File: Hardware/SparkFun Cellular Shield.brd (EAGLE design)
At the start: 53.3 x 73.7 mm, 29 parts, among them U1 ARDUINO_R3_SHIELD, U2 SPX29302, U3 SM5100B, U4 SIMHOLDER3

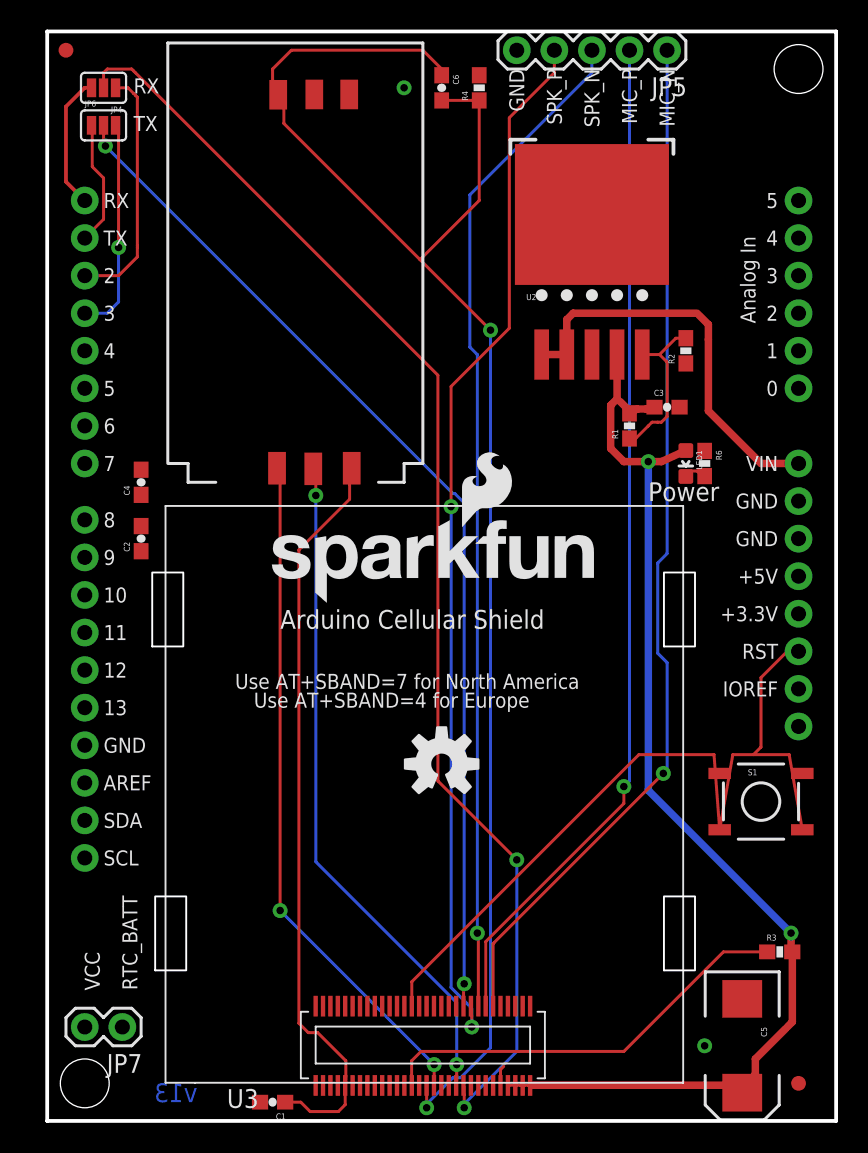
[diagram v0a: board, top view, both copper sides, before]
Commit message: Board layout cleanup
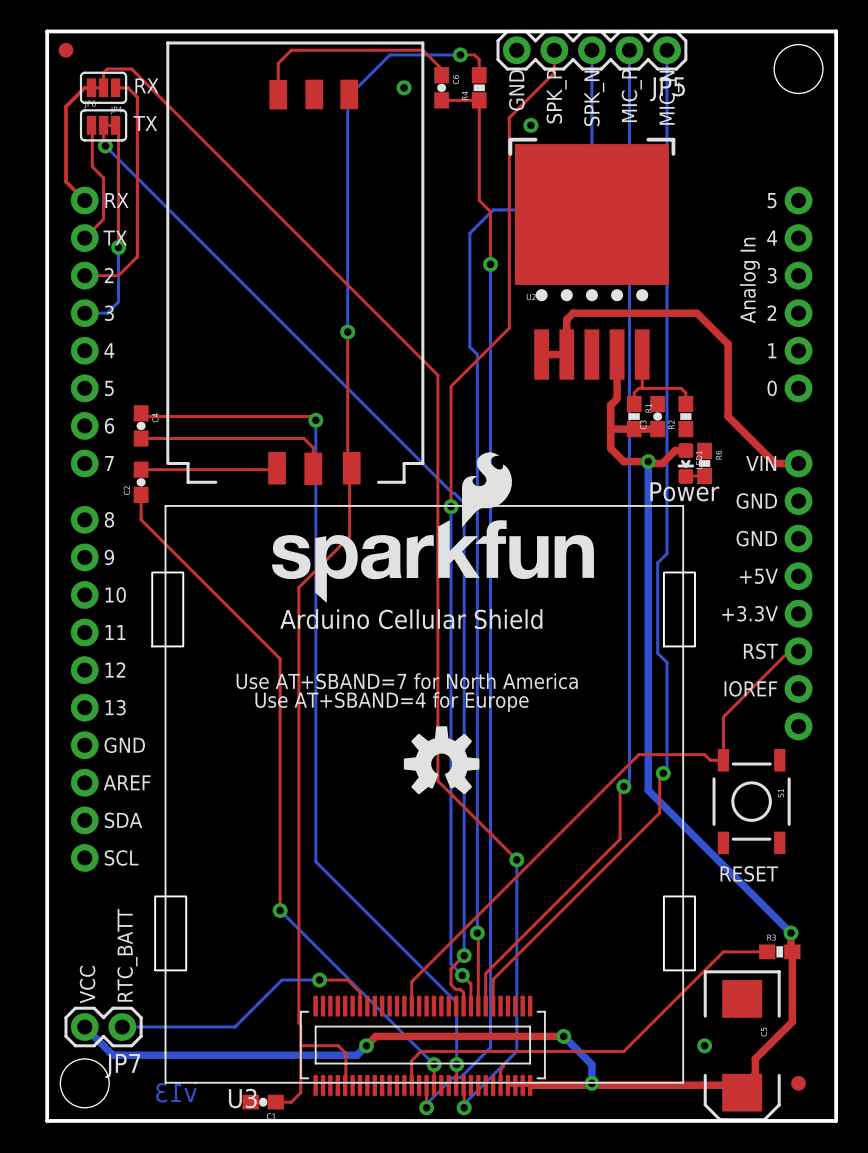
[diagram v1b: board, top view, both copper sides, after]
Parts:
- JP4, JP6: value JUMPER-PAD-3-2OF3_NC_BY_PASTE -> JUMPER-PAD-3-2OF3_NC_BY_TRACE_SMALL; device SparkFun-Passives:PAD-JUMPER-3-2OF3_NC_BY_PASTE_YES_SILK_FULL_BOX -> SparkFun-Passives:PAD-JUMPER-3-2OF3_NC_BY_TRACE_YES_SILK_FULL_BOX
- moved R2 4.45 mm to (43.2, 47.6)
- moved C2 3.81 mm to (6.35, 43.2)
- moved C4 3.81 mm to (6.35, 47.0), turned to 270 degrees
- moved C3 0.90 mm to (41.3, 47.6), turned to 90 degrees
- moved R1 0.71 mm to (39.7, 47.6), turned to 270 degrees
- moved C1 0.63 mm to (14.6, 1.27)
- moved S1 0.63 mm to (47.6, 21.6), turned to 270 degrees
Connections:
- net GND: no longer S1.2
- net RESET: no longer S1.4
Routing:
- net VCC: track 79.2 -> 117.4 mm, vias 2 -> 5
- net SIM_VCC: track 50.7 -> 87.5 mm, vias 0 -> 2
- net RTC_BATT: track 0.00 -> 18.7 mm, vias 0 -> 1
- net SIM_IO: track 91.9 -> 74.6 mm
- net RESET: track 56.4 -> 39.1 mm
- net SIM_RST: track 44.6 -> 60.9 mm
- net N$2: track 0.00 -> 13.3 mm
- net N$3: track 0.00 -> 9.23 mm
- net ADJUST: track 11.0 -> 7.55 mm
- net SPK_N: track 68.3 -> 71.6 mm
- net SIM_CLK: track 45.0 -> 48.1 mm
- net SPK_P: track 70.9 -> 68.1 mm
- net RXD0: track 69.7 -> 70.6 mm
- net VRAW: track 27.5 -> 27.0 mm
- net GND: vias 2 -> 3
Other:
- board text added: "RESET"

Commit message: Additional part updates, adding dimensions
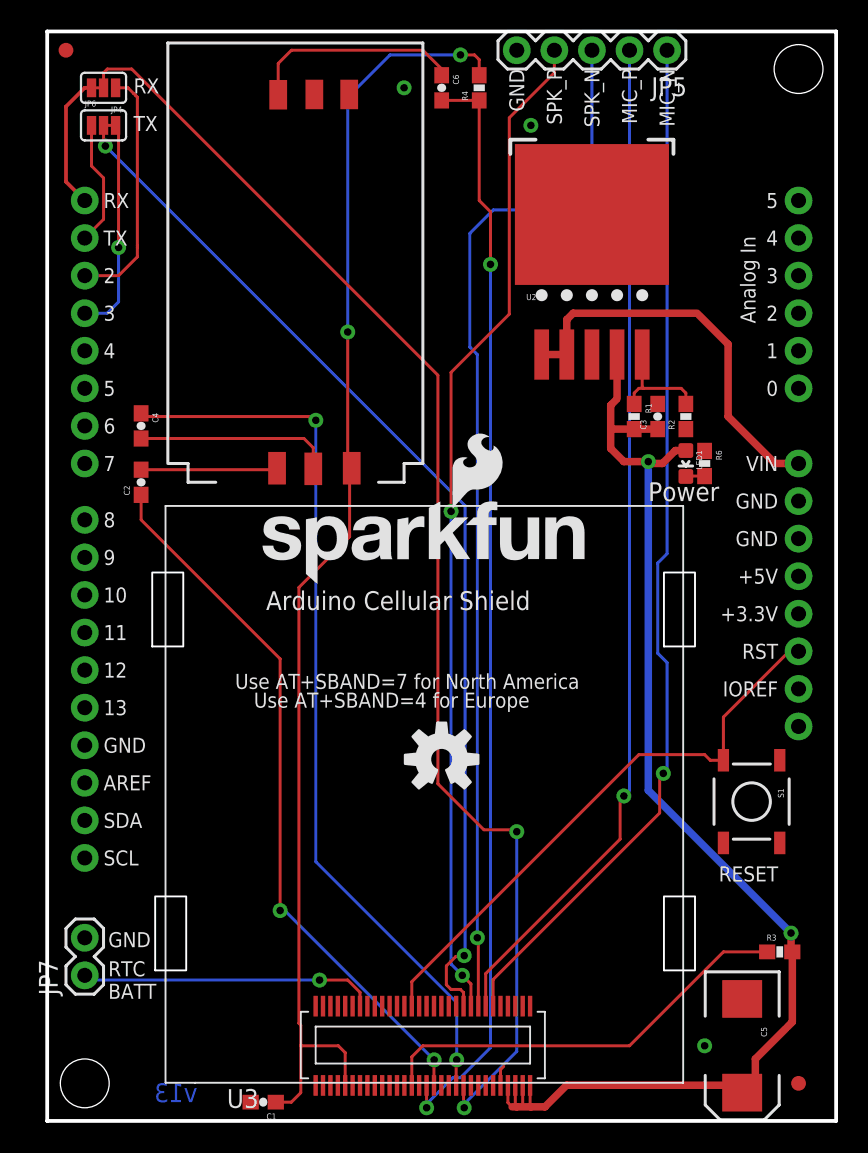
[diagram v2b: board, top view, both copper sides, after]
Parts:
- moved JP7 4.32 mm to (2.54, 9.84), turned to 90 degrees
- moved JP1 1.42 mm to (13.8, 36.2)
- moved LOGO1 0.32 mm to (26.7, 24.4)
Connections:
- net GND: now also JP7.2
- net VCC: no longer JP7.2
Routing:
- net VCC: track 117.4 -> 86.7 mm, vias 5 -> 2
- net RTC_BATT: track 18.7 -> 20.0 mm
- net TXD0: track 87.0 -> 88.3 mm
- net RXD0: track 70.6 -> 71.4 mm
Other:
- board text added: "RTC BATT"
- board text added: "Ryan Owens"
- board text removed: "Nathan Seidle"
- board text removed: "RTC_BATT"
- board text removed: "VCC"

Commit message: Updating parts with PROD IDs, fixing DRC errors w/ tKeepout on
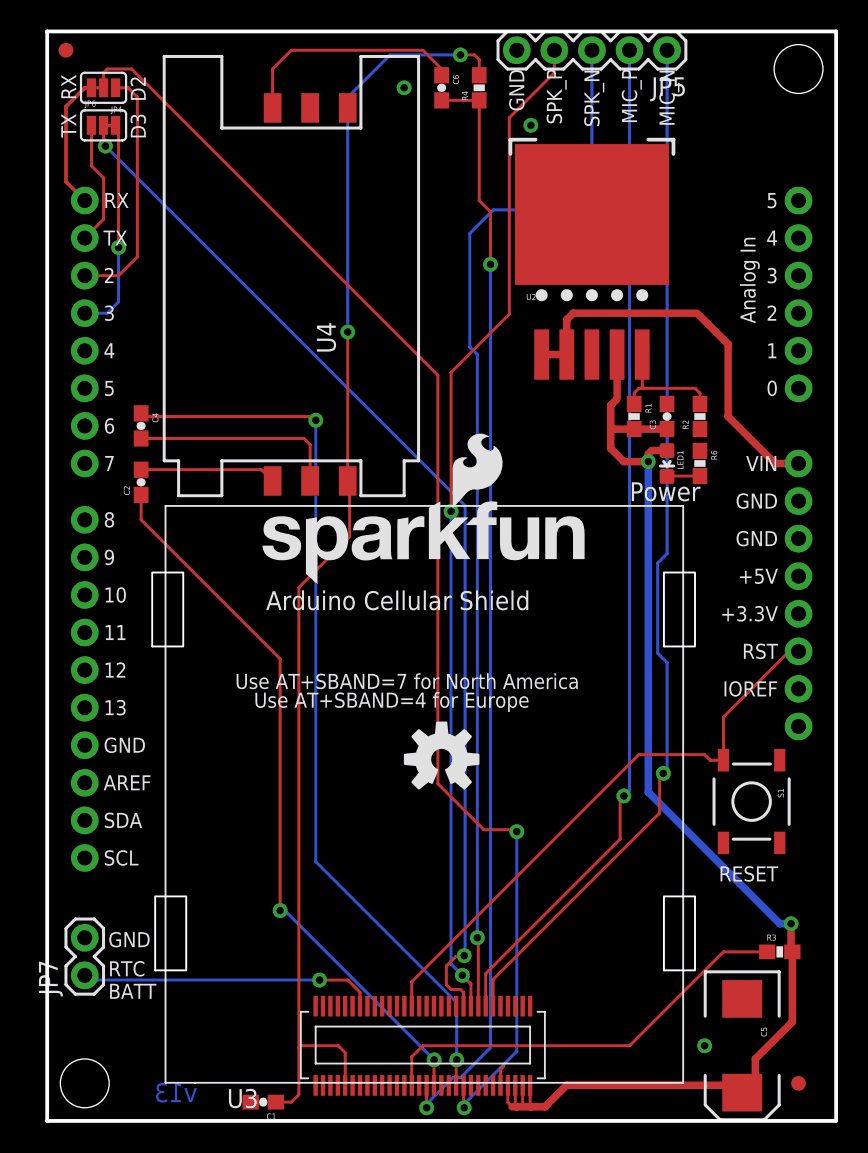
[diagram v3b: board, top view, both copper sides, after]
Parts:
- JP2, JP3: device SparkFun:FIDUCIAL-1X2 -> SparkFun-Aesthetics:FIDUCIAL-1X2
- U3: device SparkFun:SM5100B -> SparkFun-RF:SM5100B
- U4: value SIMHOLDER3 -> (none); device SparkFun:SIMHOLDER3 -> SparkFun-Connectors:SIMHOLDER
- moved U4 15.5 mm to (16.5, 55.9)
- moved LED1 1.27 mm to (41.9, 44.5)
- moved R2 0.95 mm to (44.1, 47.6)
- moved C3 0.63 mm to (41.9, 47.6)
- moved R6 0.32 mm to (44.1, 44.5)
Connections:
- net GND: now also U4.C5; no longer U4.6
- net N$1: now also U4.C7; no longer U4.4
- net N$2: now also U4.C2; no longer U4.2
- net N$3: now also U4.C3; no longer U4.3
- net SIM_VCC: now also U4.C1; no longer U4.1
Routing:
- net N$1: track 14.5 -> 15.5 mm
- net N$17: track 1.28 -> 2.23 mm
- net ADJUST: track 7.55 -> 8.51 mm
- net N$2: track 13.3 -> 14.1 mm
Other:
- board text added: "D2"
- board text added: "D3"

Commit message: Adding in 20mm battery fp for RTC
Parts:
- added BAT1: (no value), SparkFun-Electromechanical:BATTCOM_20MM_PTH
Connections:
- net GND: now also BAT1.2
- net RTC_BATT: now also BAT1.1
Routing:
- net RTC_BATT: track 20.0 -> 40.5 mm
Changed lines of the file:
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@@
 <setting verticaltext="up"/>
 </settings>
-<grid distance="0.0125" unitdist="inch" unit="inch" style="lines" multiple="1" display="yes" altdistance="0.005" altunitdist="inch" altunit="inch"/>
+<grid distance="0.05" unitdist="inch" unit="inch" style="lines" multiple="1" display="yes" altdistance="0.005" altunitdist="inch" altunit="inch"/>
 <layers>
 <layer number="1" name="Top" color="4" fill="1" visible="yes" active="yes"/>
@@
 <layer number="37" name="tTest" color="7" fill="1" visible="no" active="yes"/>
 <layer number="38" name="bTest" color="7" fill="1" visible="no" active="yes"/>
-<layer number="39" name="tKeepout" color="4" fill="11" visible="yes" active="yes"/>
-<layer number="40" name="bKeepout" color="1" fill="11" visible="yes" active="yes"/>
+<layer number="39" name="tKeepout" color="4" fill="11" visible="no" active="yes"/>
+<layer number="40" name="bKeepout" color="1" fill="11" visible="no" active="yes"/>
 <layer number="41" name="tRestrict" color="4" fill="10" visible="no" active="yes"/>
 <layer number="42" name="bRestrict" color="1" fill="10" visible="no" active="yes"/>
@@
 <layer number="47" name="Measures" color="7" fill="1" visible="no" active="yes"/>
 <layer number="48" name="Document" color="7" fill="1" visible="no" active="yes"/>
-<layer number="49" name="Reference" color="7" fill="1" visible="no" active="yes"/>
+<layer number="49" name="Reference" color="7" fill="1" visible="yes" active="yes"/>
 <layer number="50" name="dxf" color="7" fill="1" visible="no" active="yes"/>
 <layer number="51" name="tDocu" color="6" fill="1" visible="yes" active="yes"/>
@@
 <element name="STANDOFF1" library="SparkFun-Electromechanical" package="STAND-OFF" value="STAND-OFF" x="2.54" y="2.54"/>
 <element name="STANDOFF2" library="SparkFun-Electromechanical" package="STAND-OFF" value="STAND-OFF" x="50.8" y="71.12"/>
+<element name="BAT1" library="SparkFun-Electromechanical" package="BATTCOM_20MM_PTH" value="" x="24.13" y="22.86" rot="MR0"/>
 </elements>
 <signals>
@@
 <via x="32.7025" y="67.31" extent="1-16" drill="0.508"/>
 <contactref element="JP7" pad="2"/>
+<contactref element="BAT1" pad="2"/>
 </signal>
 <signal name="VCC">
@@
 <contactref element="U3" pad="5"/>
 <contactref element="R3" pad="2"/>
-<contactref element="C5" pad="A"/>
-<contactref element="U2" pad="4"/>
-<contactref element="R1" pad="2"/>
-<contactref element="C3" pad="1"/>
-<contactref element="LED1" pad="A"/>
 <wire x1="47.879" y1="4.191" x2="49.911" y2="6.223" width="0.508" layer="1"/>
 <wire x1="40.64" y1="22.225" x2="40.64" y2="44.577" width="0.508" layer="16"/>
 <wire x1="50.292" y1="11.938" x2="50.292" y2="13.335" width="0.508" layer="1"/>
-<wire x1="38.53" y1="48.846" x2="38.53" y2="51.815" width="0.508" layer="1"/>
 <wire x1="40.64" y1="44.577" x2="38.989" y2="44.577" width="0.508" layer="1"/>
 <wire x1="38.989" y1="44.577" x2="38.1" y2="45.466" width="0.508" layer="1"/>
@@
 <via x="40.64" y="44.577" extent="1-16" drill="0.508"/>
 <via x="50.292" y="13.335" extent="1-16" drill="0.508"/>
-<wire x1="39.6875" y1="46.775" x2="41.91" y2="46.775" width="0.508" layer="1"/>
-<wire x1="39.6875" y1="46.775" x2="38.2025" y2="46.775" width="0.508" layer="1"/>
 <wire x1="38.2025" y1="46.775" x2="38.1" y2="46.6725" width="0.508" layer="1"/>
 <wire x1="40.767" y1="44.45" x2="40.64" y2="44.577" width="0.508" layer="1"/>
@@
 <wire x1="31.75" y1="0.9525" x2="32.0675" y2="0.9525" width="0.2032" layer="1"/>
 <wire x1="32.0675" y1="0.9525" x2="32.15" y2="1.035" width="0.2032" layer="1"/>
-<wire x1="46.487" y1="2.413" x2="46.99" y2="1.91" width="0.508" layer="1"/>
 <wire x1="47.879" y1="4.191" x2="47.879" y2="2.799" width="0.508" layer="1"/>
-<wire x1="47.879" y1="2.799" x2="46.99" y2="1.91" width="0.508" layer="1"/>
 <wire x1="50.292" y1="11.938" x2="50.292" y2="11.518" width="0.2032" layer="1"/>
 <wire x1="50.292" y1="11.518" x2="50.38" y2="11.43" width="0.2032" layer="1"/>
-<wire x1="35.1155" y1="2.413" x2="46.487" y2="2.413" width="0.508" layer="1"/>
+<wire x1="35.1155" y1="2.413" x2="47.493" y2="2.413" width="0.508" layer="1"/>
 <wire x1="40.64" y1="22.225" x2="49.53" y2="13.335" width="0.508" layer="16"/>
 <wire x1="49.53" y1="13.335" x2="50.292" y2="13.335" width="0.508" layer="16"/>
-<wire x1="41.91" y1="45.327" x2="40.882" y2="45.327" width="0.508" layer="1"/>
 <wire x1="40.882" y1="45.327" x2="40.64" y2="45.085" width="0.508" layer="1"/>
 <wire x1="40.64" y1="45.085" x2="40.64" y2="44.577" width="0.508" layer="1"/>
+<contactref element="C3" pad="1"/>
+<contactref element="LED1" pad="A"/>
+<contactref element="U2" pad="4"/>
+<contactref element="R1" pad="2"/>
+<contactref element="C5" pad="A"/>
+<wire x1="38.53" y1="48.846" x2="38.53" y2="51.815" width="0.508" layer="1"/>
+<wire x1="38.2025" y1="46.775" x2="39.6875" y2="46.775" width="0.508" layer="1"/>
+<wire x1="40.882" y1="45.327" x2="41.91" y2="45.327" width="0.508" layer="1"/>
+<wire x1="41.91" y1="45.327" x2="41.91" y2="46.775" width="0.508" layer="1"/>
+<wire x1="47.493" y1="2.413" x2="47.879" y2="2.799" width="0.508" layer="1"/>
+<wire x1="46.99" y1="1.91" x2="47.493" y2="2.413" width="0.508" layer="1"/>
 </signal>
 <signal name="BOOT">
@@
 <wire x1="18.415" y1="9.525" x2="2.8575" y2="9.525" width="0.2032" layer="16"/>
 <wire x1="2.8575" y1="9.525" x2="2.54" y2="9.8425" width="0.2032" layer="16"/>
+<contactref element="BAT1" pad="1"/>
+<wire x1="12.28" y1="22.86" x2="12.28" y2="14.185" width="0.508" layer="1"/>
+<wire x1="12.28" y1="14.185" x2="7.62" y2="9.525" width="0.508" layer="1"/>
+<wire x1="7.62" y1="9.525" x2="2.8575" y2="9.525" width="0.508" layer="1"/>
+<wire x1="2.8575" y1="9.525" x2="2.54" y2="9.8425" width="0.508" layer="1"/>
 </signal>
 <signal name="N$1">

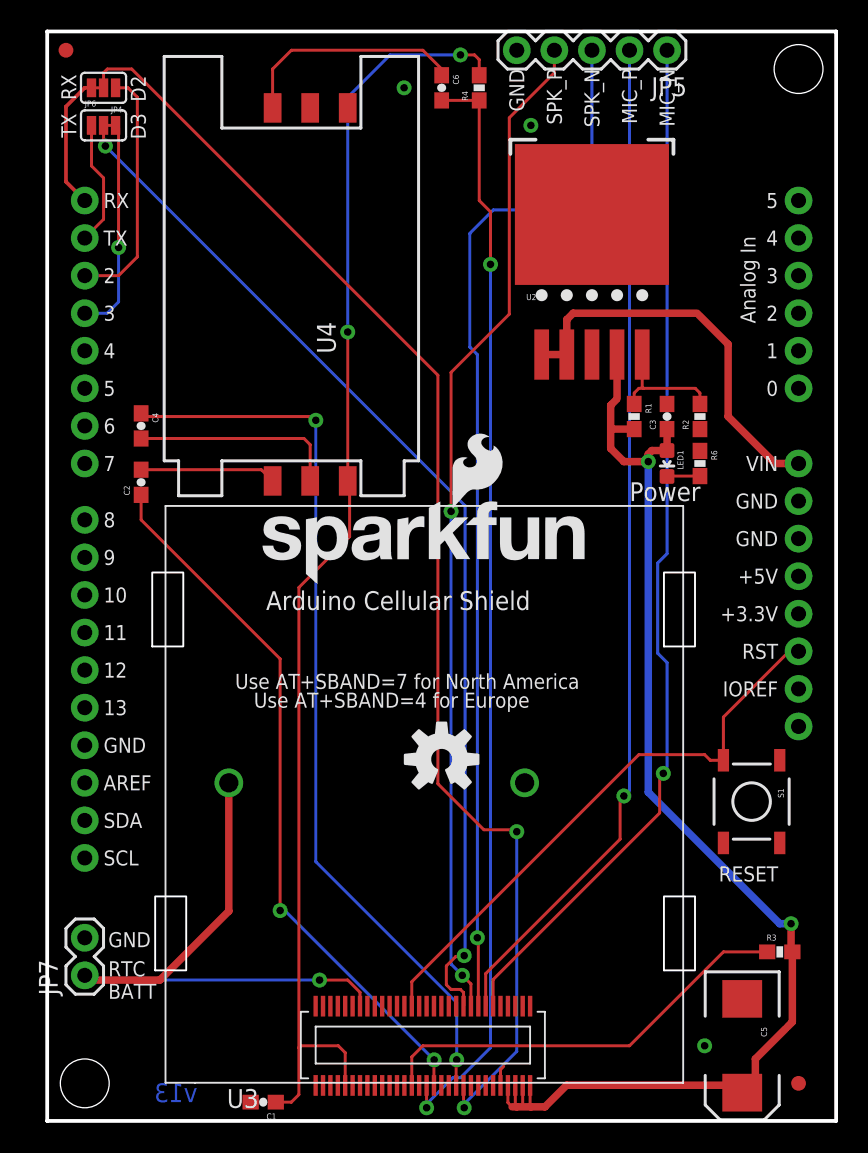
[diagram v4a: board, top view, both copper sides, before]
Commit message: Adding fixes from QC checklist
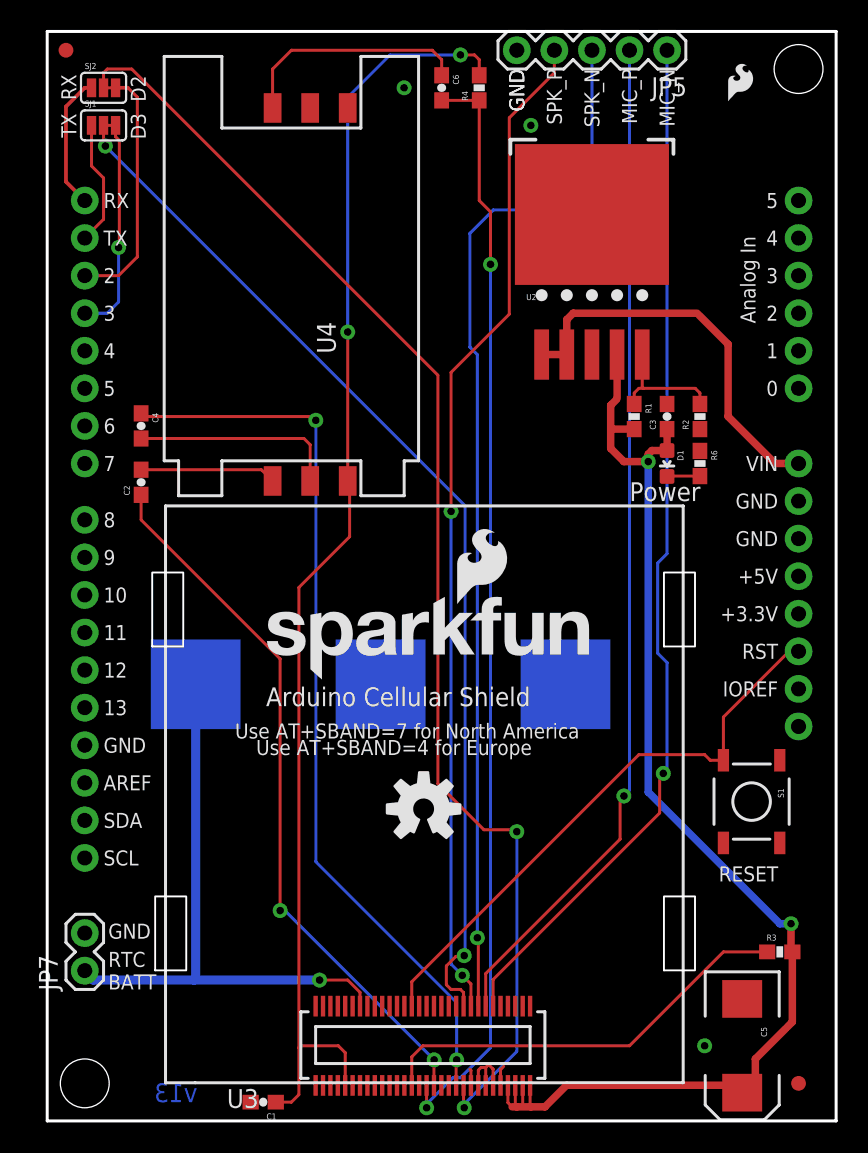
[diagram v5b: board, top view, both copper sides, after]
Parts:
- added LOGO2: SFE_LOGO_FLAME.1_INCH, SparkFun-Aesthetics:SFE_LOGO_FLAME_.1
- BAT1: device SparkFun-Electromechanical:BATTCOM_20MM_PTH -> SparkFun-Electromechanical:BATTCON_20MM
- moved BAT1 6.85 mm to (22.5, 29.5), turned to 180 degrees
- moved JP1 6.46 mm to (14.1, 29.7)
- moved LOGO1 3.57 mm to (25.5, 21.1)
- moved JP7 0.32 mm to (2.54, 10.2)
- turned SJ2 to 0 degrees
- renumbered JP4 to SJ2, JP6 to SJ1, LED1 to D1
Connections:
- removed net A0: U1.A0
- removed net A1: U1.A1
- removed net A2: U1.A2
- removed net A3: U1.A3
- removed net A4: U1.A4
- removed net A5: U1.A5
- removed net D10: U1.D10
- removed net D11: U1.D11
- removed net D12: U1.D12
- removed net D13: U1.D13
- removed net D4: U1.D4
- removed net D5: U1.D5
- removed net D6: U1.D6
- removed net D7: U1.D7
- removed net D8: U1.D8
- removed net D9: U1.D9
- net D-RX: now also SJ2.3; no longer SJ2.1
- net RX-I: now also SJ2.1; no longer SJ2.3
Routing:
- net GND: track 1.37 -> 7.13 mm
